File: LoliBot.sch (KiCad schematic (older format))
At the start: 24 parts

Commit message: Added footprint for lolibot-lite
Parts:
- removed J? (x2): CONN_01X13, symbol CONN_01X13
- added U1: LOLIN32-LITE, symbol LOLIN32-LITE
- gave numbers to parts that had none: 22
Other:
- note removed: "WEMOS LOLIN32 LITE"

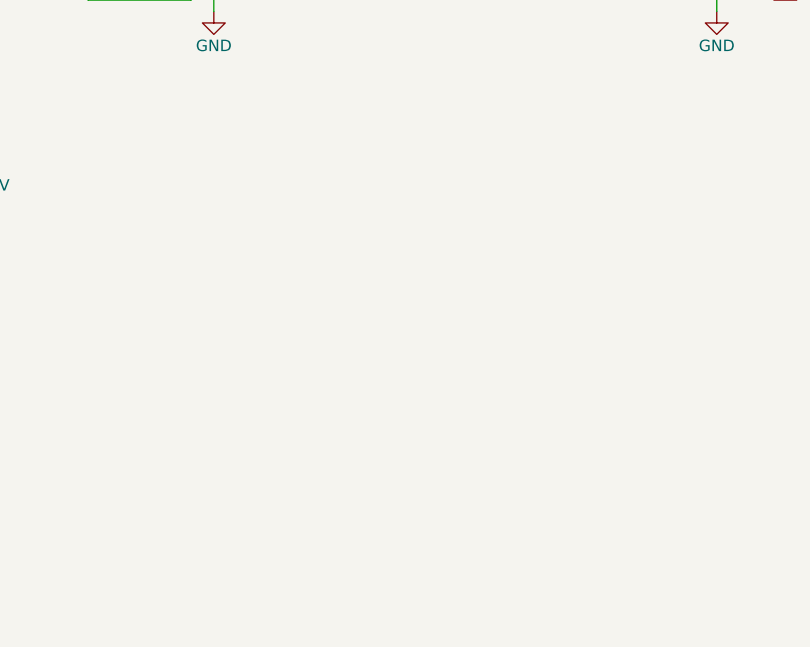
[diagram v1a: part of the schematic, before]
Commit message: Added mpu-9250 module header and updated power pins.
* Fixes to the l9110 library for power input
* Fixes to the lolin32-lite library for power output
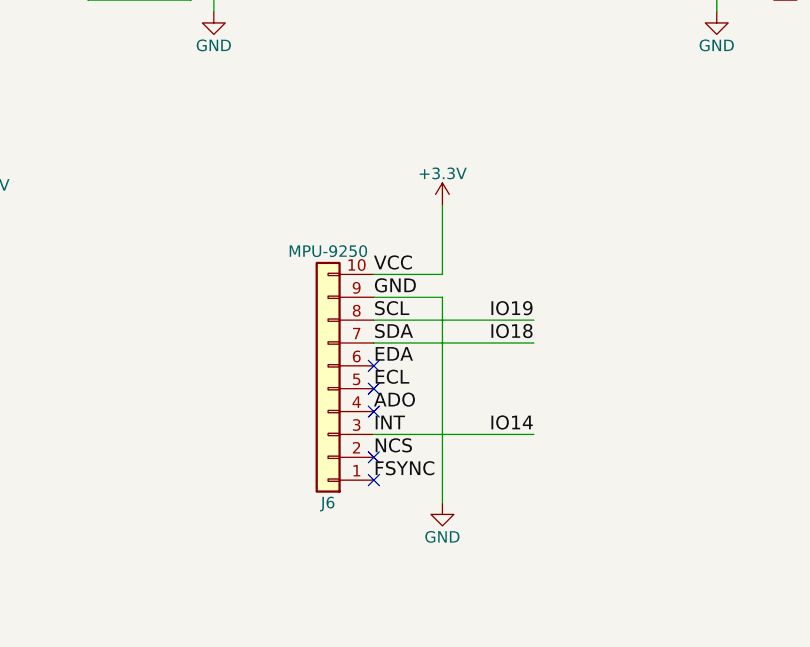
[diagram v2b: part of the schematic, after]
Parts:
- added J6: MPU-9250, symbol Conn_01x10
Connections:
- net +3V3: now also J6.10 (Pin_10)
- net GND: now also J6.9 (Pin_9)
- net IO18: now also J6.7 (Pin_7)
- net IO19: now also J6.8 (Pin_8)
- net IO14 renamed INT
- net INT: now also J6.3 (Pin_3)
- new net ADO: J6.4 (Pin_4)
- new net ECL: J6.5 (Pin_5)
- new net EDA: J6.6 (Pin_6)
- new net FSYNC: J6.1 (Pin_1)
- new net NCS: J6.2 (Pin_2)
- no-connect marks 1 -> 6
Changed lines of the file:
@@
 $EndComp
 $Comp
-L GND #PWR1
+L GND #PWR01
 U 1 1 59DB6136
 P 1250 2150
-F 0 "#PWR1" H 1250 1900 50  0001 C CNN
+F 0 "#PWR01" H 1250 1900 50  0001 C CNN
 F 1 "GND" H 1250 2000 50  0000 C CNN
 F 2 "" H 1250 2150 50  0001 C CNN
@@
 $EndComp
 $Comp
-L GND #PWR3
+L GND #PWR02
 U 1 1 59DB694D
 P 2900 1800
-F 0 "#PWR3" H 2900 1550 50  0001 C CNN
+F 0 "#PWR02" H 2900 1550 50  0001 C CNN
 F 1 "GND" H 2900 1650 50  0000 C CNN
 F 2 "" H 2900 1800 50  0001 C CNN
@@
 	3300 2100 3300 2200
 $Comp
-L GND #PWR4
+L GND #PWR03
 U 1 1 59DB6ABB
 P 3300 2200
-F 0 "#PWR4" H 3300 1950 50  0001 C CNN
+F 0 "#PWR03" H 3300 1950 50  0001 C CNN
 F 1 "GND" H 3300 2050 50  0000 C CNN
 F 2 "" H 3300 2200 50  0001 C CNN
@@
 NoConn ~ 5300 1850
 $Comp
-L GND #PWR9
+L GND #PWR04
 U 1 1 59DB708D
 P 5400 2250
-F 0 "#PWR9" H 5400 2000 50  0001 C CNN
+F 0 "#PWR04" H 5400 2000 50  0001 C CNN
 F 1 "GND" H 5400 2100 50  0000 C CNN
 F 2 "" H 5400 2250 50  0001 C CNN
@@
 $EndComp
 $Comp
-L GND #PWR7
+L GND #PWR05
 U 1 1 59DB70B0
 P 4150 2150
-F 0 "#PWR7" H 4150 1900 50  0001 C CNN
+F 0 "#PWR05" H 4150 1900 50  0001 C CNN
 F 1 "GND" H 4150 2000 50  0000 C CNN
 F 2 "" H 4150 2150 50  0001 C CNN
@@
 Connection ~ 5700 1550
 $Comp
-L GND #PWR10
+L GND #PWR06
 U 1 1 59DB7D00
 P 5700 2250
-F 0 "#PWR10" H 5700 2000 50  0001 C CNN
+F 0 "#PWR06" H 5700 2000 50  0001 C CNN
 F 1 "GND" H 5700 2100 50  0000 C CNN
 F 2 "" H 5700 2250 50  0001 C CNN
@@
 	6050 1250 6050 2250
 $Comp
-L GND #PWR11
+L GND #PWR07
 U 1 1 59DB7E46
 P 6050 2250
-F 0 "#PWR11" H 6050 2000 50  0001 C CNN
+F 0 "#PWR07" H 6050 2000 50  0001 C CNN
 F 1 "GND" H 6050 2100 50  0000 C CNN
 F 2 "" H 6050 2250 50  0001 C CNN
@@
 $EndComp
 $Comp
-L GND #PWR15
+L GND #PWR08
 U 1 1 59DB834E
 P 7200 2250
-F 0 "#PWR15" H 7200 2000 50  0001 C CNN
+F 0 "#PWR08" H 7200 2000 50  0001 C CNN
 F 1 "GND" H 7200 2100 50  0000 C CNN
 F 2 "" H 7200 2250 50  0001 C CNN
@@
 	7200 1650 7200 2250
 $Comp
-L +5V #PWR14
+L +5V #PWR09
 U 1 1 59DB92E1
 P 7200 750
-F 0 "#PWR14" H 7200 600 50  0001 C CNN
+F 0 "#PWR09" H 7200 600 50  0001 C CNN
 F 1 "+5V" H 7200 890 50  0000 C CNN
 F 2 "" H 7200 750 50  0001 C CNN
@@
 $EndComp
 $Comp
-L +5V #PWR6
+L +5V #PWR010
 U 1 1 59DBA2B8
 P 3750 3250
-F 0 "#PWR6" H 3750 3100 50  0001 C CNN
+F 0 "#PWR010" H 3750 3100 50  0001 C CNN
 F 1 "+5V" H 3750 3390 50  0000 C CNN
 F 2 "" H 3750 3250 50  0001 C CNN
@@
 $EndComp
 $Comp
-L GND #PWR8
+L GND #PWR011
 U 1 1 59DBA675
 P 4300 3550
-F 0 "#PWR8" H 4300 3300 50  0001 C CNN
+F 0 "#PWR011" H 4300 3300 50  0001 C CNN
 F 1 "GND" H 4300 3400 50  0000 C CNN
 F 2 "" H 4300 3550 50  0001 C CNN
@@
 $EndComp
 $Comp
-L GND #PWR18
+L GND #PWR012
 U 1 1 59DBB61B
 P 10450 4750
-F 0 "#PWR18" H 10450 4500 50  0001 C CNN
+F 0 "#PWR012" H 10450 4500 50  0001 C CNN
 F 1 "GND" H 10450 4600 50  0000 C CNN
 F 2 "" H 10450 4750 50  0001 C CNN
@@
 	10850 4250 10850 4600
 $Comp
-L +5V #PWR16
+L +5V #PWR013
 U 1 1 59DBBC2C
 P 8950 3950
-F 0 "#PWR16" H 8950 3800 50  0001 C CNN
+F 0 "#PWR013" H 8950 3800 50  0001 C CNN
 F 1 "+5V" H 8950 4090 50  0000 C CNN
 F 2 "" H 8950 3950 50  0001 C CNN
@@
 $EndComp
 $Comp
-L GND #PWR19
+L GND #PWR014
 U 1 1 59DBCDC3
 P 10500 6050
-F 0 "#PWR19" H 10500 5800 50  0001 C CNN
+F 0 "#PWR014" H 10500 5800 50  0001 C CNN
 F 1 "GND" H 10500 5900 50  0000 C CNN
 F 2 "" H 10500 6050 50  0001 C CNN
@@
 	10900 5550 10900 5900
 $Comp
-L +5V #PWR17
+L +5V #PWR015
 U 1 1 59DBCDD1
 P 9000 5250
-F 0 "#PWR17" H 9000 5100 50  0001 C CNN
+F 0 "#PWR015" H 9000 5100 50  0001 C CNN
 F 1 "+5V" H 9000 5390 50  0000 C CNN
 F 2 "" H 9000 5250 50  0001 C CNN
@@
 $EndComp
 $Comp
-L +5V #PWR12
+L +5V #PWR016
 U 1 1 59DBDAEB
 P 6500 3150
-F 0 "#PWR12" H 6500 3000 50  0001 C CNN
+F 0 "#PWR016" H 6500 3000 50  0001 C CNN
 F 1 "+5V" H 6500 3290 50  0000 C CNN
 F 2 "" H 6500 3150 50  0001 C CNN
@@
 $EndComp
 $Comp
-L GND #PWR13
+L GND #PWR017
 U 1 1 59DBDB38
 P 6500 3550
-F 0 "#PWR13" H 6500 3300 50  0001 C CNN
+F 0 "#PWR017" H 6500 3300 50  0001 C CNN
 F 1 "GND" H 6500 3400 50  0000 C CNN
 F 2 "" H 6500 3550 50  0001 C CNN
@@
 IO13
 $Comp
-L +3.3V #PWR5
+L +3.3V #PWR018
 U 1 1 59DC0699
 P 3300 4450
-F 0 "#PWR5" H 3300 4300 50  0001 C CNN
+F 0 "#PWR018" H 3300 4300 50  0001 C CNN
 F 1 "+3.3V" H 3300 4590 50  0000 C CNN
 F 2 "" H 3300 4450 50  0001 C CNN
@@
 $EndComp
 $Comp
-L GND #PWR2
+L GND #PWR019
 U 1 1 59DC0B2B
 P 1300 6000
-F 0 "#PWR2" H 1300 5750 50  0001 C CNN
+F 0 "#PWR019" H 1300 5750 50  0001 C CNN
 F 1 "GND" H 1300 5850 50  0000 C CNN
 F 2 "" H 1300 6000 50  0001 C CNN
@@
 	1    0    0    -1
 $EndComp
+$Comp
+L Conn_01x10 J6
+U 1 1 59E28CBB
+P 4800 5200
+F 0 "J6" H 4800 5700 50  0000 C CNN
+F 1 "MPU-9250" H 4800 4600 50  0000 C CNN
+F 2 "" H 4800 5200 50  0001 C CNN
+F 3 "" H 4800 5200 50  0001 C CNN
+	1    4800 5200
+	-1   0    0    1
+$EndComp
+Text Label 5000 4700 0    60   ~ 0
+VCC
+Text Label 5000 4800 0    60   ~ 0
+GND
+Text Label 5000 4900 0    60   ~ 0
+SCL
+Text Label 5000 5000 0    60   ~ 0
+SDA
+Text Label 5000 5100 0    60   ~ 0
+EDA
+Text Label 5000 5200 0    60   ~ 0
+ECL
+Text Label 5000 5300 0    60   ~ 0
+ADO
+Text Label 5000 5400 0    60   ~ 0
+INT
+Text Label 5000 5500 0    60   ~ 0
+NCS
+Text Label 5000 5600 0    60   ~ 0
+FSYNC
+$Comp
+L +3.3V #PWR020
+U 1 1 59E28F97
+P 5300 4400
+F 0 "#PWR020" H 5300 4250 50  0001 C CNN
+F 1 "+3.3V" H 5300 4540 50  0000 C CNN
+F 2 "" H 5300 4400 50  0001 C CNN
+F 3 "" H 5300 4400 50  0001 C CNN
+	1    5300 4400
+	1    0    0    -1
+$EndComp
+Wire Wire Line
+	5000 4700 5300 4700
+Wire Wire Line
+	5300 4700 5300 4400
+$Comp
+L GND #PWR021
+U 1 1 59E29073
+P 5300 5700
+F 0 "#PWR021" H 5300 5450 50  0001 C CNN
+F 1 "GND" H 5300 5550 50  0000 C CNN
+F 2 "" H 5300 5700 50  0001 C CNN
+F 3 "" H 5300 5700 50  0001 C CNN
+	1    5300 5700
+	1    0    0    -1
+$EndComp
+Wire Wire Line
+	5000 4800 5300 4800
+Wire Wire Line
+	5300 4800 5300 5700
+Wire Wire Line
+	5000 4900 5700 4900
+Wire Wire Line
+	5000 5000 5700 5000
+Text Label 5700 4900 2    60   ~ 0
+IO19
+Text Label 5700 5000 2    60   ~ 0
+IO18
+Wire Wire Line
+	5000 5400 5700 5400
+Text Label 5700 5400 2    60   ~ 0
+IO14
+NoConn ~ 5000 5600
+NoConn ~ 5000 5500
+NoConn ~ 5000 5300
+NoConn ~ 5000 5200
+NoConn ~ 5000 5100
 $EndSCHEMATC

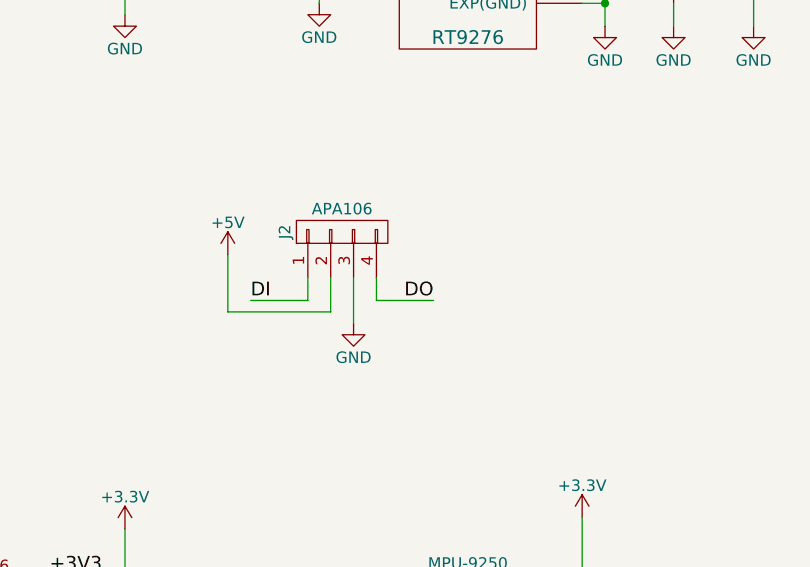
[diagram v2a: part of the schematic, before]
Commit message: Assigned some footprints and built out apa106 chain for underlights.
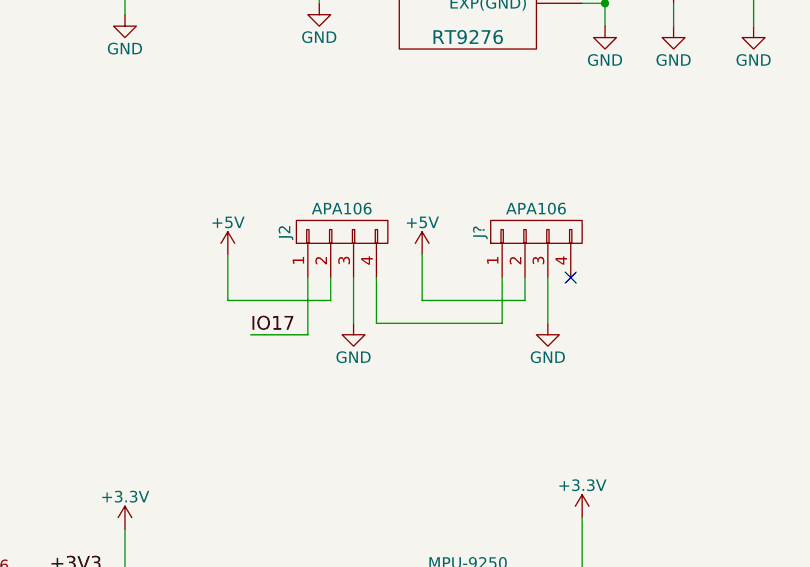
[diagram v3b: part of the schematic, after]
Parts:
- added J?: APA106, symbol CONN_01X04
- J4, J5: footprint (none) -> Connectors_JST:JST_PH_B2B-PH-K_02x2.00mm_Straight
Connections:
- net DI is gone; now on net IO17: J2.1 (P1)
- net +5V: now also J?.2 (P2)
- net GND: now also J?.3 (P3)
- net DO: no longer names the net of J2.4 (P4)
- net DO: now also J?.1 (P1)
- no-connect marks 6 -> 7
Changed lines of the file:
@@
 $EndComp
-Wire Wire Line
-	4200 3350 4200 3500
-Wire Wire Line
-	4200 3500 3750 3500
-Wire Wire Line
-	3750 3500 3750 3250
 Wire Wire Line
 	4300 3350 4300 3550
-Wire Wire Line
-	4100 3350 4100 3450
-Wire Wire Line
-	4100 3450 3850 3450
-Wire Wire Line
-	4400 3350 4400 3450
-Wire Wire Line
-	4400 3450 4650 3450
-Text Label 3850 3450 0    60   ~ 0
-DI
-Text Label 4650 3450 2    60   ~ 0
-DO
 $Comp
 L L9110 U3
@@
 F 0 "J4" H 10800 4950 50  0000 C CNN
 F 1 "RIGHT" V 10900 4800 50  0000 C CNN
-F 2 "" H 10800 4800 50  0001 C CNN
+F 2 "Connectors_JST:JST_PH_B2B-PH-K_02x2.00mm_Straight" H 10800 4800 50  0001 C CNN
 F 3 "" H 10800 4800 50  0001 C CNN
 	1    10800 4800
@@
 F 0 "J5" H 10850 6250 50  0000 C CNN
 F 1 "LEFT" V 10950 6100 50  0000 C CNN
-F 2 "" H 10850 6100 50  0001 C CNN
+F 2 "Connectors_JST:JST_PH_B2B-PH-K_02x2.00mm_Straight" H 10850 6100 50  0001 C CNN
 F 3 "" H 10850 6100 50  0001 C CNN
 	1    10850 6100
@@
 NoConn ~ 5000 5200
 NoConn ~ 5000 5100
+$Comp
+L CONN_01X04 J?
+U 1 1 59E30588
+P 5100 3150
+F 0 "J?" H 5100 3400 50  0000 C CNN
+F 1 "APA106" V 5200 3150 50  0000 C CNN
+F 2 "" H 5100 3150 50  0001 C CNN
+F 3 "" H 5100 3150 50  0001 C CNN
+	1    5100 3150
+	0    -1   -1   0
+$EndComp
+Wire Wire Line
+	4400 3350 4400 3550
+Wire Wire Line
+	4400 3550 4950 3550
+Wire Wire Line
+	4950 3550 4950 3350
+Wire Wire Line
+	4100 3600 4100 3350
+Wire Wire Line
+	3850 3600 4100 3600
+Text Label 3850 3600 0    60   ~ 0
+IO17
+$Comp
+L +5V #PWR?
+U 1 1 59E30CAE
+P 4600 3250
+F 0 "#PWR?" H 4600 3100 50  0001 C CNN
+F 1 "+5V" H 4600 3390 50  0000 C CNN
+F 2 "" H 4600 3250 50  0001 C CNN
+F 3 "" H 4600 3250 50  0001 C CNN
+	1    4600 3250
+	1    0    0    -1
+$EndComp
+Wire Wire Line
+	5050 3350 5050 3450
+Wire Wire Line
+	5050 3450 4600 3450
+Wire Wire Line
+	4600 3450 4600 3250
+Wire Wire Line
+	4200 3350 4200 3450
+Wire Wire Line
+	4200 3450 3750 3450
+Wire Wire Line
+	3750 3450 3750 3250
+Wire Wire Line
+	5150 3350 5150 3550
+$Comp
+L GND #PWR?
+U 1 1 59E30F3C
+P 5150 3550
+F 0 "#PWR?" H 5150 3300 50  0001 C CNN
+F 1 "GND" H 5150 3400 50  0000 C CNN
+F 2 "" H 5150 3550 50  0001 C CNN
+F 3 "" H 5150 3550 50  0001 C CNN
+	1    5150 3550
+	1    0    0    -1
+$EndComp
+NoConn ~ 5250 3350
 $EndSCHEMATC

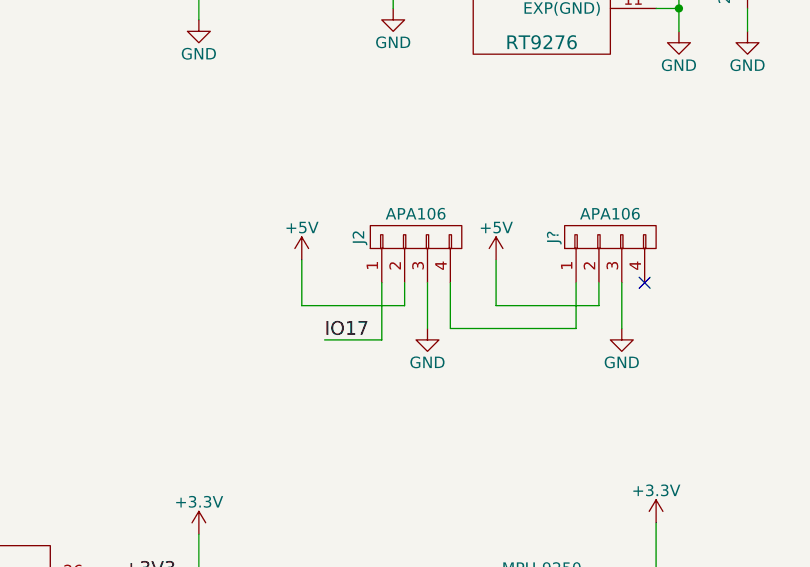
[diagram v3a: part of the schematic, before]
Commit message: Added datasheets and started assigning footprints.
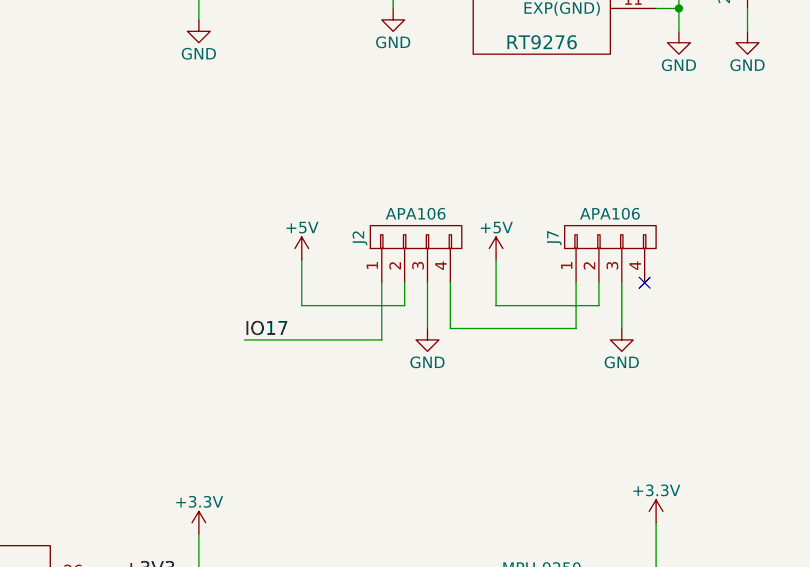
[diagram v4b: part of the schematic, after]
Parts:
- U2: footprint (none) -> Housings_DFN_QFN:DFN-10-1EP_3x3mm_Pitch0.5mm
- gave numbers to parts that had none: 1
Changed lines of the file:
@@
 F 0 "SW1" H 2300 1250 50  0000 C CNN
 F 1 "SPST" H 2300 1050 50  0000 C CNN
-F 2 "" H 2300 1150 50  0000 C CNN
+F 2 "" H 2300 1150 50  0001 C CNN
 F 3 "" H 2300 1150 50  0000 C CNN
 	1    2300 1150
@@
 F 0 "U2" H 4800 2300 60  0000 C CNN
 F 1 "RT9276" H 4800 1300 60  0000 C CNN
-F 2 "" H 4750 1750 60  0001 C CNN
+F 2 "Housings_DFN_QFN:DFN-10-1EP_3x3mm_Pitch0.5mm" H 4750 1750 60  0001 C CNN
 F 3 "" H 4750 1750 60  0001 C CNN
 	1    4800 1800
@@
 F 0 "U3" H 9700 4550 60  0000 C CNN
 F 1 "L9110" H 9700 3950 60  0000 C CNN
-F 2 "" H 9700 4300 60  0000 C CNN
+F 2 "" H 9700 4300 60  0001 C CNN
 F 3 "" H 9700 4300 60  0000 C CNN
 	1    9700 4300
@@
 F 0 "U4" H 9750 5850 60  0000 C CNN
 F 1 "L9110" H 9750 5250 60  0000 C CNN
-F 2 "" H 9750 5600 60  0000 C CNN
+F 2 "" H 9750 5600 60  0001 C CNN
 F 3 "" H 9750 5600 60  0000 C CNN
 	1    9750 5600
@@
 NoConn ~ 5000 5100
 $Comp
-L CONN_01X04 J?
+L CONN_01X04 J7
 U 1 1 59E30588
 P 5100 3150
-F 0 "J?" H 5100 3400 50  0000 C CNN
+F 0 "J7" H 5100 3400 50  0000 C CNN
 F 1 "APA106" V 5200 3150 50  0000 C CNN
 F 2 "" H 5100 3150 50  0001 C CNN
@@
 	4100 3600 4100 3350
 Wire Wire Line
-	3850 3600 4100 3600
-Text Label 3850 3600 0    60   ~ 0
+	3500 3600 4100 3600
+Text Label 3500 3600 0    60   ~ 0
 IO17
 $Comp
-L +5V #PWR?
+L +5V #PWR022
 U 1 1 59E30CAE
 P 4600 3250
-F 0 "#PWR?" H 4600 3100 50  0001 C CNN
+F 0 "#PWR022" H 4600 3100 50  0001 C CNN
 F 1 "+5V" H 4600 3390 50  0000 C CNN
 F 2 "" H 4600 3250 50  0001 C CNN
@@
 	5150 3350 5150 3550
 $Comp
-L GND #PWR?
+L GND #PWR023
 U 1 1 59E30F3C
 P 5150 3550
-F 0 "#PWR?" H 5150 3300 50  0001 C CNN
+F 0 "#PWR023" H 5150 3300 50  0001 C CNN
 F 1 "GND" H 5150 3400 50  0000 C CNN
 F 2 "" H 5150 3550 50  0001 C CNN
